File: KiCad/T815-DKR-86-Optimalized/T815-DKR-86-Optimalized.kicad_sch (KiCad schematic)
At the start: 44 parts, among them J1 PWM Steering, J2 PWM Throttle, J3 PWM 3.ch.button, M1 RC Model Motor, Q1 BS170, Q3 BS170, Q4 BS170, Q6 BS170, Q7 BS170, U1 ESC - regulator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

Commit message: schema update - rearanged pins.
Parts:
- added SW1: SW_Calibration, LED_THT:LED_D2.0mm_W4.8mm_H2.5mm_FlatTop, symbol Switch:SW_DIP_x01
- A1: footprint Module:Arduino_Nano -> FootPrintProjectLibrary:Arduino_Nano
- Q1, Q3, Q4: footprint Package_TO_SOT_THT:TO-92L_Inline_Wide -> FootPrintProjectLibrary:BS170-TO-92L_Inline_Wide
- U3: footprint (none) -> FootPrintProjectLibrary:Izolační modul s optočlenem
- renumbered Q-Ramp to Q-Ramp1
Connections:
- net GND: now also SW1.2
- net at Q4.1 (G): now also A1.21 (A2); no longer A1.11 (D8)
- net at Q1.1 (G): now also A1.23 (A4); no longer A1.22 (A3)
- net at A1.19 (A0): now also SW1.1
- net at A1.20 (A1): no longer U3.4 (OUT)
- net at Q3.1 (G): now also A1.22 (A3); no longer A1.21 (A2)
- net at A1.24 (A5): now also U3.4 (OUT)
- no-connect marks 18 -> 17

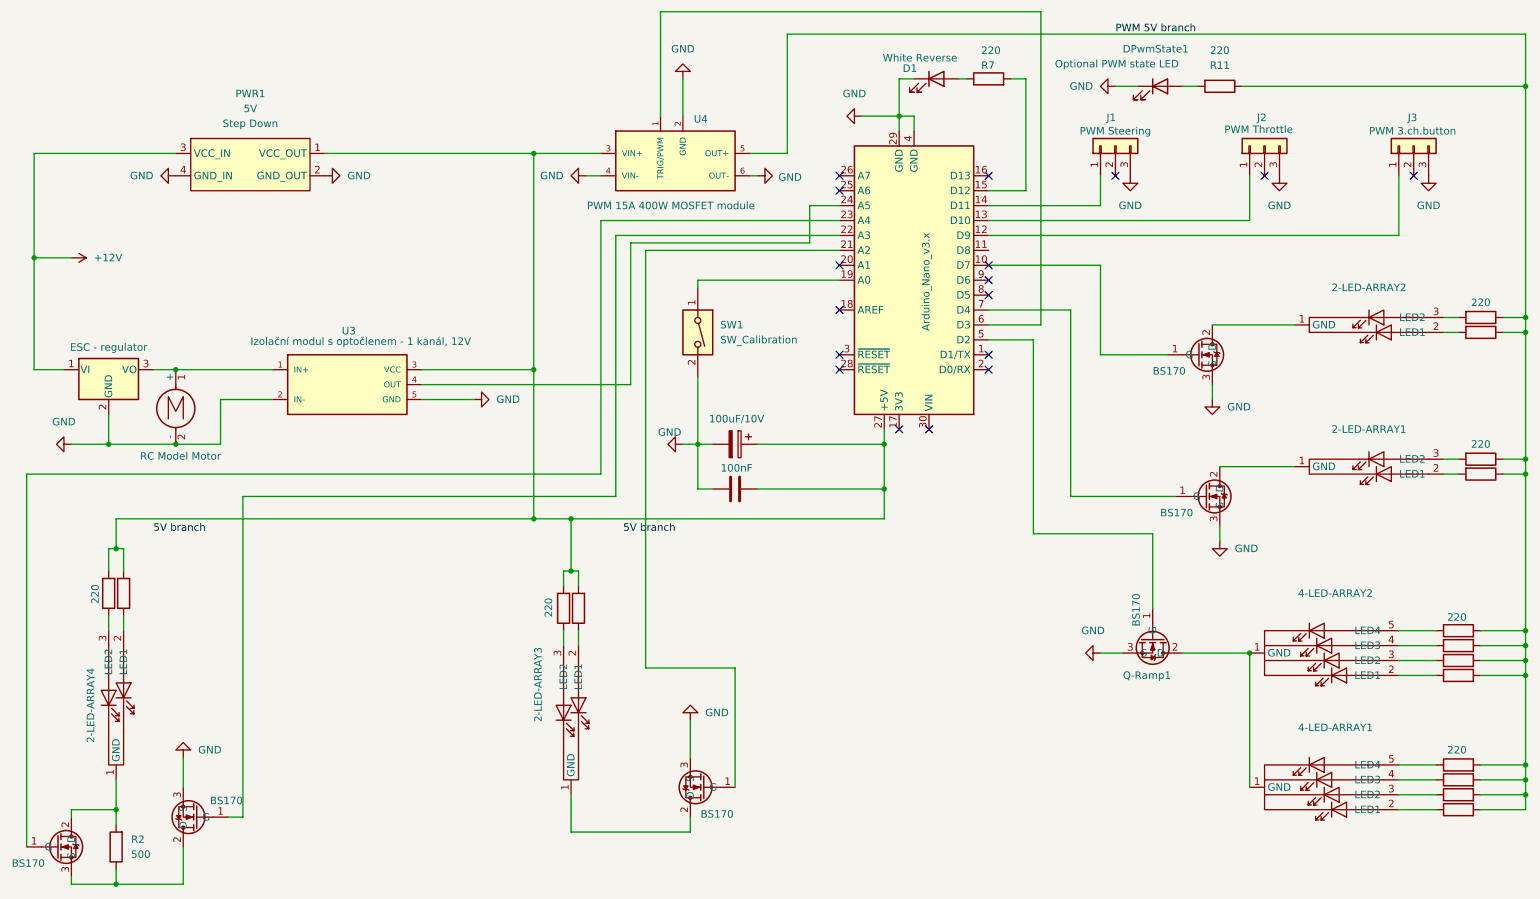
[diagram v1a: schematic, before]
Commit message: schema update - pcb more optima use of arduino pins
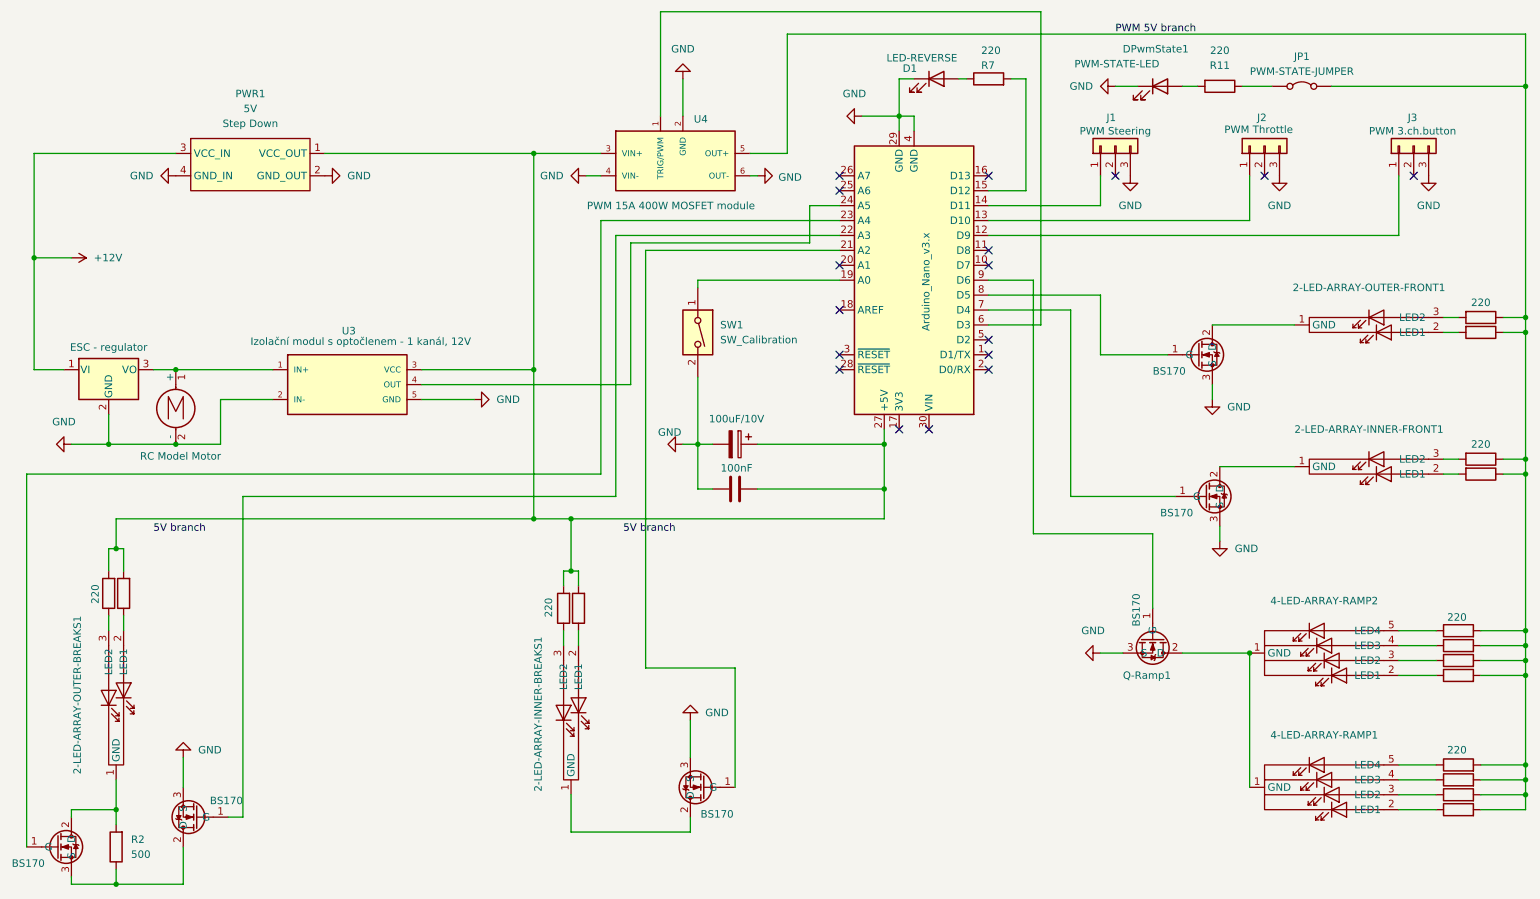
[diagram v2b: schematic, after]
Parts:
- added JP1: PWM-STATE-JUMPER, symbol Jumper:Jumper_2_Bridged
- D1: value White Reverse -> LED-REVERSE
- DPwmState1: value Optional PWM state LED -> PWM-STATE-LED
- Q-Ramp1: footprint Package_TO_SOT_THT:TO-92L_Inline_Wide -> FootPrintProjectLibrary:BS170-TO-92L_Inline_Wide
- renumbered 2-LED-ARRAY3 to 2-LED-ARRAY-INNER-BREAKS1, 2-LED-ARRAY1 to 2-LED-ARRAY-INNER-FRONT1, 2-LED-ARRAY4 to 2-LED-ARRAY-OUTER-BREAKS1, 2-LED-ARRAY2 to 2-LED-ARRAY-OUTER-FRONT1, 4-LED-ARRAY1 to 4-LED-ARRAY-RAMP1, 4-LED-ARRAY2 to 4-LED-ARRAY-RAMP2
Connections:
- net PWM 5V branch: now also JP1.2 (B); no longer R11.1
- net at Q-Ramp1.1 (G): now also A1.9 (D6); no longer A1.5 (D2)
- net at A1.10 (D7): no longer Q6.1 (G)
- net at A1.8 (D5): now also Q6.1 (G)
- new net: JP1.1 (A), R11.1
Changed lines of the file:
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@@
 	)
 	(no_connect
-		(at 187.96 67.31)
+		(at 187.96 62.23)
 	)
 	(no_connect
@@
 	)
 	(no_connect
+		(at 187.96 77.47)
+	)
+	(no_connect
 		(at 162.56 49.53)
 	)
@@
 		(at 187.96 64.77)
 	)
-	(no_connect
-		(at 187.96 69.85)
-	)
 	(wire
 		(pts
@@
 	(wire
 		(pts
-			(xy 187.96 77.47) (xy 195.58 77.47)
+			(xy 201.93 72.39) (xy 201.93 104.14)
 		)
 		(stroke
@@
 	(wire
 		(pts
-			(xy 201.93 72.39) (xy 201.93 104.14)
+			(xy 166.37 39.37) (xy 172.72 39.37)
 		)
 		(stroke
@@
 	(wire
 		(pts
-			(xy 166.37 39.37) (xy 172.72 39.37)
+			(xy 57.15 87.63) (xy 57.15 95.25)
 		)
 		(stroke
@@
 	(wire
 		(pts
-			(xy 57.15 87.63) (xy 57.15 95.25)
+			(xy 226.06 85.09) (xy 226.06 87.63)
 		)
 		(stroke
@@
 	(wire
 		(pts
-			(xy 226.06 85.09) (xy 226.06 87.63)
+			(xy 116.84 107.95) (xy 116.84 116.84)
 		)
 		(stroke
@@
 	(wire
 		(pts
-			(xy 116.84 107.95) (xy 116.84 116.84)
+			(xy 271.78 152.4) (xy 279.4 152.4)
 		)
 		(stroke
@@
 	(wire
 		(pts
-			(xy 271.78 152.4) (xy 279.4 152.4)
+			(xy 279.4 127) (xy 279.4 129.54)
 		)
 		(stroke
@@
 	(wire
 		(pts
-			(xy 279.4 127) (xy 279.4 129.54)
+			(xy 246.38 34.29) (xy 279.4 34.29)
 		)
 		(stroke
@@
 	(wire
 		(pts
-			(xy 207.01 64.77) (xy 187.96 64.77)
+			(xy 201.93 104.14) (xy 219.71 104.14)
 		)
 		(stroke
@@
 	(wire
 		(pts
-			(xy 201.93 104.14) (xy 219.71 104.14)
+			(xy 215.9 110.49) (xy 215.9 123.19)
 		)
 		(stroke
@@
 	(wire
 		(pts
-			(xy 215.9 110.49) (xy 215.9 123.19)
+			(xy 187.96 69.85) (xy 207.01 69.85)
 		)
 		(stroke
@@
 	(wire
 		(pts
-			(xy 195.58 110.49) (xy 195.58 77.47)
+			(xy 187.96 67.31) (xy 195.58 67.31)
 		)
 		(stroke
@@
 	(wire
 		(pts
-			(xy 207.01 80.01) (xy 207.01 64.77)
+			(xy 207.01 80.01) (xy 207.01 69.85)
 		)
 		(stroke
@@
 	(wire
 		(pts
+			(xy 195.58 67.31) (xy 195.58 110.49)
+		)
+		(stroke
+			(width 0)
+			(type default)
+		)
+	)
+	(wire
+		(pts
 			(xy 40.64 124.46) (xy 40.64 127)
 		)
@@
 	(wire
 		(pts
-			(xy 231.14 34.29) (xy 279.4 34.29)
+			(xy 231.14 34.29) (xy 236.22 34.29)
 		)
 		(stroke
@@
 			)
 		)
-		(property "Value" "White Reverse"
+		(property "Value" "LED-REVERSE"
 			(at 182.626 29.464 0)
 			(effects
@@
 			)
 		)
-		(property "Footprint" "Package_TO_SOT_THT:TO-92L_Inline_Wide"
+		(property "Footprint" "FootPrintProjectLibrary:BS170-TO-92L_Inline_Wide"
 			(at 213.995 133.35 0)
 			(effects
@@
 		(dnp no)
 		(fields_autoplaced yes)
-		(property "Reference" "4-LED-ARRAY1"
-			(at 247.015 143.51 0)
+		(property "Reference" "4-LED-ARRAY-RAMP1"
+			(at 245.11 144.78 0)
 			(effects
 				(font
@@
 		)
 		(property "Value" "~"
-			(at 247.015 146.05 0)
+			(at 245.11 147.32 0)
 			(effects
 				(font
@@
 			(project "T815-DKR-86-Optimalized"
 				(path "/7a98be5d-3389-447b-a56a-164f9b5d3bd8"
-					(reference "4-LED-ARRAY1")
+					(reference "4-LED-ARRAY-RAMP1")
 					(unit 1)
 				)
@@
 		(on_board yes)
 		(dnp no)
-		(property "Reference" "2-LED-ARRAY4"
-			(at 35.052 133.35 0)
+		(property "Reference" "2-LED-ARRAY-OUTER-BREAKS1"
+			(at 32.766 124.46 0)
 			(effects
 				(font
@@
 			(project "T815-DKR-86-Optimalized"
 				(path "/7a98be5d-3389-447b-a56a-164f9b5d3bd8"
-					(reference "2-LED-ARRAY4")
+					(reference "2-LED-ARRAY-OUTER-BREAKS1")
 					(unit 1)
 				)
@@
 		(dnp no)
 		(fields_autoplaced yes)
-		(property "Reference" "2-LED-ARRAY2"
+		(property "Reference" "2-LED-ARRAY-OUTER-FRONT1"
 			(at 252.73 68.58 0)
 			(effects
@@
 			(project "T815-DKR-86-Optimalized"
 				(path "/7a98be5d-3389-447b-a56a-164f9b5d3bd8"
-					(reference "2-LED-ARRAY2")
+					(reference "2-LED-ARRAY-OUTER-FRONT1")
 					(unit 1)
 				)
@@
 			)
 		)
-		(property "Value" "Optional PWM state LED"
+		(property "Value" "PWM-STATE-LED"
 			(at 209.804 30.48 0)
 			(effects
@@
 	)
 	(symbol
+		(lib_id "Jumper:Jumper_2_Bridged")
+		(at 241.3 34.29 0)
+		(unit 1)
+		(exclude_from_sim yes)
+		(in_bom yes)
+		(on_board yes)
+		(dnp no)
+		(fields_autoplaced yes)
+		(property "Reference" "JP1"
+			(at 241.3 29.21 0)
+			(effects
+				(font
+					(size 1.27 1.27)
+				)
+			)
+		)
+		(property "Value" "PWM-STATE-JUMPER"
+			(at 241.3 31.75 0)
+			(effects
+				(font
+					(size 1.27 1.27)
+				)
+			)
+		)
+		(property "Footprint" ""
+			(at 241.3 34.29 0)
+			(effects
+				(font
+					(size 1.27 1.27)
+				)
+				(hide yes)
+			)
+		)
+		(property "Datasheet" "~"
+			(at 241.3 34.29 0)
+			(effects
+				(font
+					(size 1.27 1.27)
+				)
+				(hide yes)
+			)
+		)
+		(property "Description" "Jumper, 2-pole, closed/bridged"
+			(at 241.3 34.29 0)
+			(effects
+				(font
+					(size 1.27 1.27)
+				)
+				(hide yes)
+			)
+		)
+		(pin "1"
+		)
+		(pin "2"
+		)
+		(instances
+			(project "T815-DKR-86-Optimalized"
+				(path "/7a98be5d-3389-447b-a56a-164f9b5d3bd8"
+					(reference "JP1")
+					(unit 1)
+				)
+			)
+		)
+	)
+	(symbol
 		(lib_id "Device:R")
 		(at 187.96 33.02 90)
@@
 		(dnp no)
 		(fields_autoplaced yes)
-		(property "Reference" "4-LED-ARRAY2"
-			(at 247.015 120.65 0)
+		(property "Reference" "4-LED-ARRAY-RAMP2"
+			(at 245.11 121.92 0)
 			(effects
 				(font
@@
 		)
 		(property "Value" "~"
-			(at 247.015 123.19 0)
+			(at 245.11 124.46 0)
 			(effects
 				(font
@@
 			(project "T815-DKR-86-Optimalized"
 				(path "/7a98be5d-3389-447b-a56a-164f9b5d3bd8"
-					(reference "4-LED-ARRAY2")
+					(reference "4-LED-ARRAY-RAMP2")
 					(unit 1)
 				)
@@
 		(dnp no)
 		(fields_autoplaced yes)
-		(property "Reference" "2-LED-ARRAY1"
+		(property "Reference" "2-LED-ARRAY-INNER-FRONT1"
 			(at 252.73 92.71 0)
 			(effects
@@
 			(project "T815-DKR-86-Optimalized"
 				(path "/7a98be5d-3389-447b-a56a-164f9b5d3bd8"
-					(reference "2-LED-ARRAY1")
+					(reference "2-LED-ARRAY-INNER-FRONT1")
 					(unit 1)
 				)
@@
 		(on_board yes)
 		(dnp no)
-		(property "Reference" "2-LED-ARRAY3"
-			(at 111.252 129.794 0)
+		(property "Reference" "2-LED-ARRAY-INNER-BREAKS1"
+			(at 111.252 128.016 0)
 			(effects
 				(font
@@
 			(project "T815-DKR-86-Optimalized"
 				(path "/7a98be5d-3389-447b-a56a-164f9b5d3bd8"
-					(reference "2-LED-ARRAY3")
+					(reference "2-LED-ARRAY-INNER-BREAKS1")
 					(unit 1)
 				)

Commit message: none
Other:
- moved on the sheet: 2-LED-ARRAY-OUTER-BREAKS1
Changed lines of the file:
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@@
 	(wire
 		(pts
-			(xy 40.64 124.46) (xy 40.64 127)
+			(xy 40.64 124.46) (xy 40.64 128.27)
 		)
 		(stroke
@@
 	(wire
 		(pts
-			(xy 39.37 152.4) (xy 39.37 157.48)
+			(xy 39.37 153.67) (xy 39.37 157.48)
 		)
 		(stroke
@@
 	(wire
 		(pts
-			(xy 38.1 124.46) (xy 38.1 127)
+			(xy 38.1 124.46) (xy 38.1 128.27)
 		)
 		(stroke
@@
 		(lib_name "2xLed_XH-3A_3")
 		(lib_id "T815-DKR-86:2xLed_XH-3A")
-		(at 39.37 137.16 270)
+		(at 39.37 138.43 270)
 		(unit 1)
 		(exclude_from_sim no)
@@
 		(dnp no)
 		(property "Reference" "2-LED-ARRAY-OUTER-BREAKS1"
-			(at 32.766 124.46 0)
+			(at 32.766 125.73 0)
 			(effects
 				(font
@@
 		)
 		(property "Value" "~"
-			(at 43.18 140.97 90)
+			(at 43.18 142.24 90)
 			(effects
 				(font
@@
 		)
 		(property "Footprint" "Connector_JST:JST_XH_B3B-XH-A_1x03_P2.50mm_Vertical"
-			(at 30.48 134.62 0)
+			(at 30.48 135.89 0)
 			(effects
 				(font
@@
 		)
 		(property "Datasheet" ""
-			(at 30.48 134.62 0)
+			(at 30.48 135.89 0)
 			(effects
 				(font
@@
 		)
 		(property "Description" "2x LED Array"
-			(at 30.48 134.62 0)
-			(effects
-				(font
+			(at 30.48 135.89 0)
+			(effects
+				(font

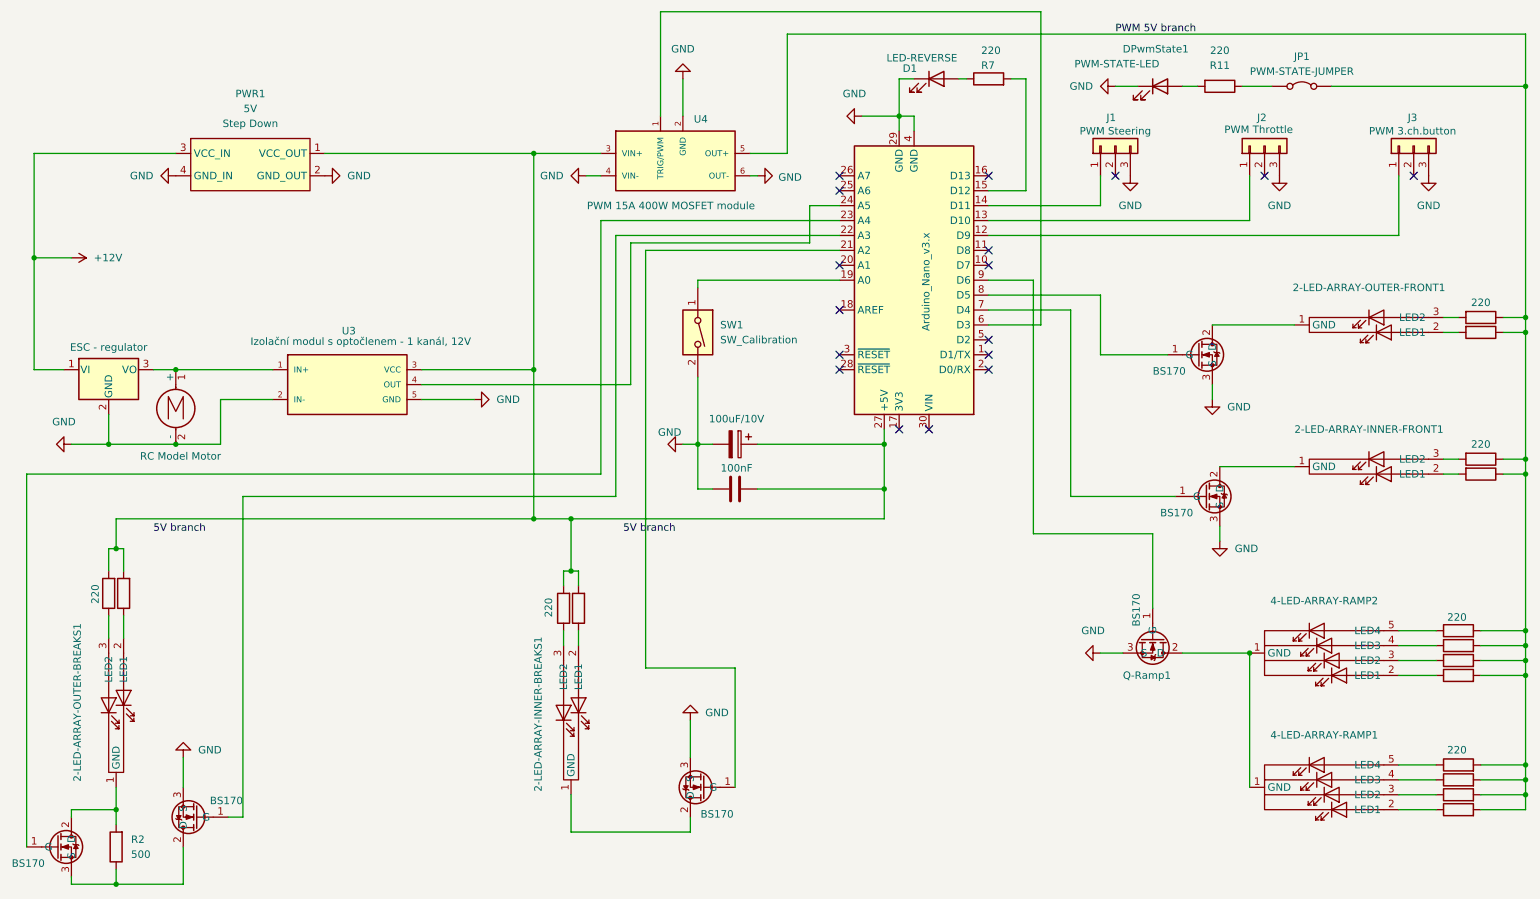
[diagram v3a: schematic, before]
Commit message: Changed pins numbers usage to respond with physical HW layout.
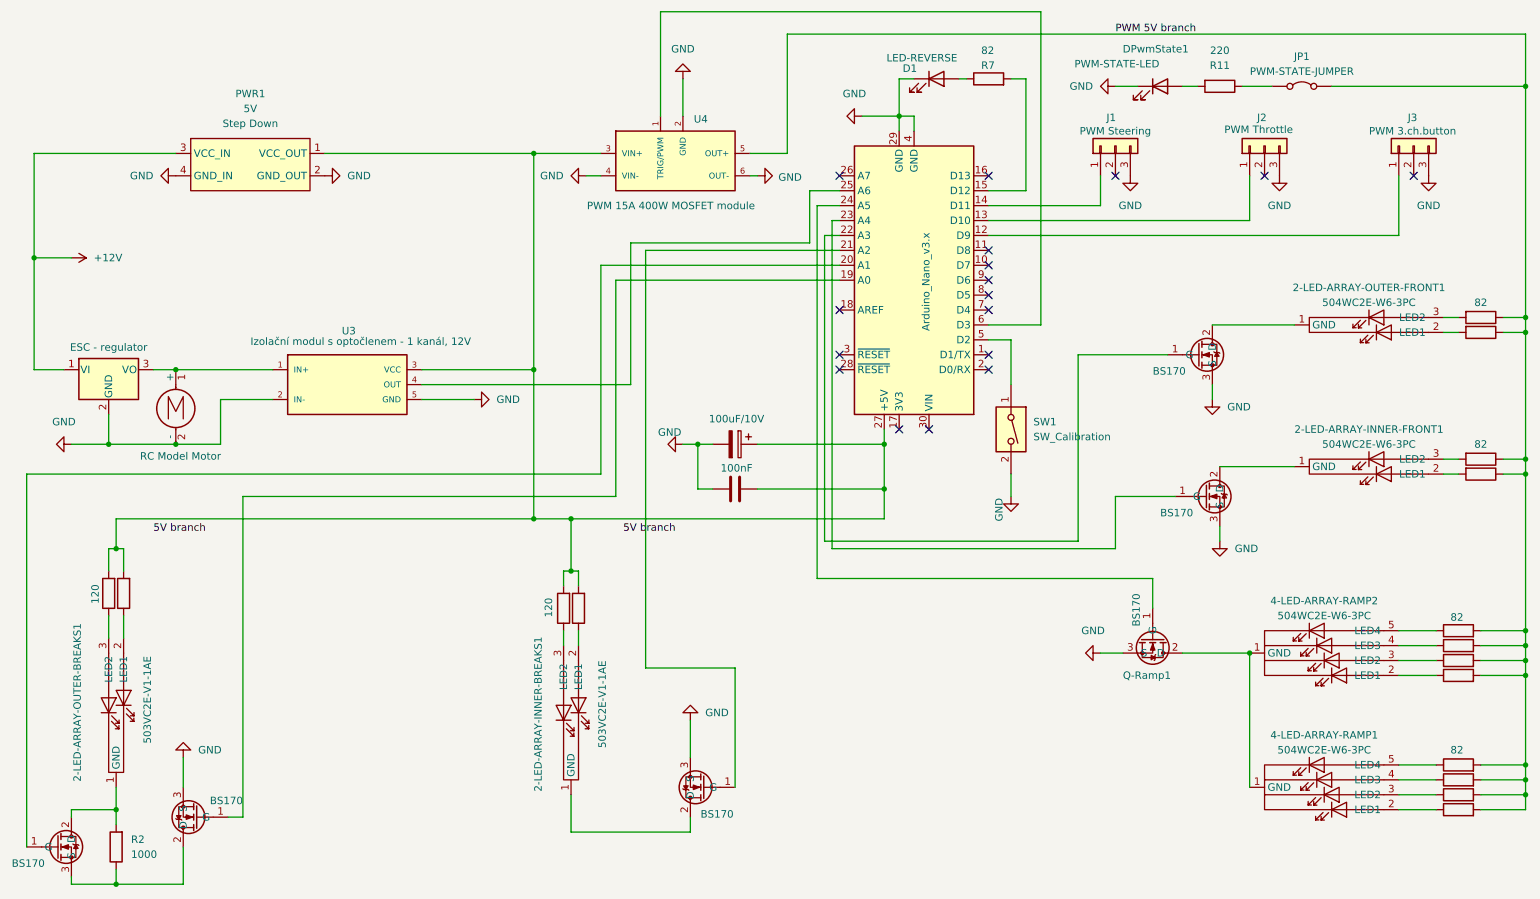
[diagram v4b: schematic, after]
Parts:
- 2-LED-ARRAY-INNER-BREAKS1, 2-LED-ARRAY-OUTER-BREAKS1: value ~ -> 503VC2E-V1-1AE
- 2-LED-ARRAY-INNER-FRONT1, 2-LED-ARRAY-OUTER-FRONT1, 4-LED-ARRAY-RAMP1, 4-LED-ARRAY-RAMP2: value ~ -> 504WC2E-W6-3PC
- R1, R3, R5, R6: value 220 -> 120
- R10, R12, R13, R14, R15, R16, R17, R18, R19, R20, R7, R8, R9: value 220 -> 82
- R2: value 500 -> 1000
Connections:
- net at Q-Ramp1.1 (G): now also A1.24 (A5); no longer A1.9 (D6)
- net at Q1.1 (G): now also A1.20 (A1); no longer A1.23 (A4)
- net at A1.19 (A0): now also Q3.1 (G); no longer SW1.1
- net at A1.22 (A3): now also Q6.1 (G); no longer Q3.1 (G)
- net at U3.4 (OUT): now also A1.25 (A6); no longer A1.24 (A5)
- net at A1.5 (D2): now also SW1.1
- net at Q7.1 (G): now also A1.23 (A4); no longer A1.7 (D4)
- net at A1.8 (D5): no longer Q6.1 (G)
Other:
- moved on the sheet: SW1
